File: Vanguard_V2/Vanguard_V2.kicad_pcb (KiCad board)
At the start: 4 copper layers, 55.9 x 30.5 mm, 77 parts, among them IC1 ST1L05CPU33R, IC2 MAX-M10S-00B, IC3 ADXL375BCCZ-RL, IC4 ASM330LHHTR, J1 Conn_01x02_Pin, J2 Conn_01x05_Pin, J3 MEM2067-02-180-00-A, J4 Conn_01x04_Pin, J5 Conn_01x02_Pin, J6 Screw_Terminal_01x04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

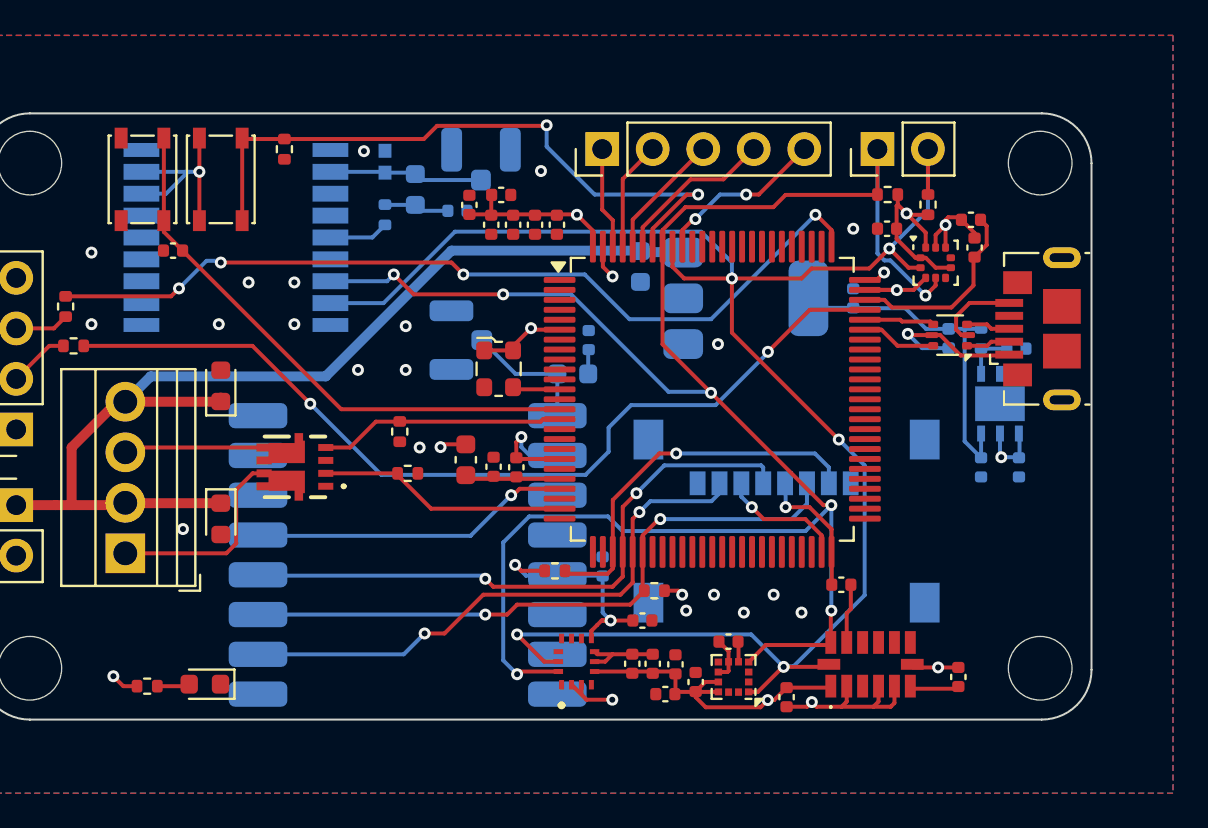
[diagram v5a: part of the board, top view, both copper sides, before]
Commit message: Added ejection charges
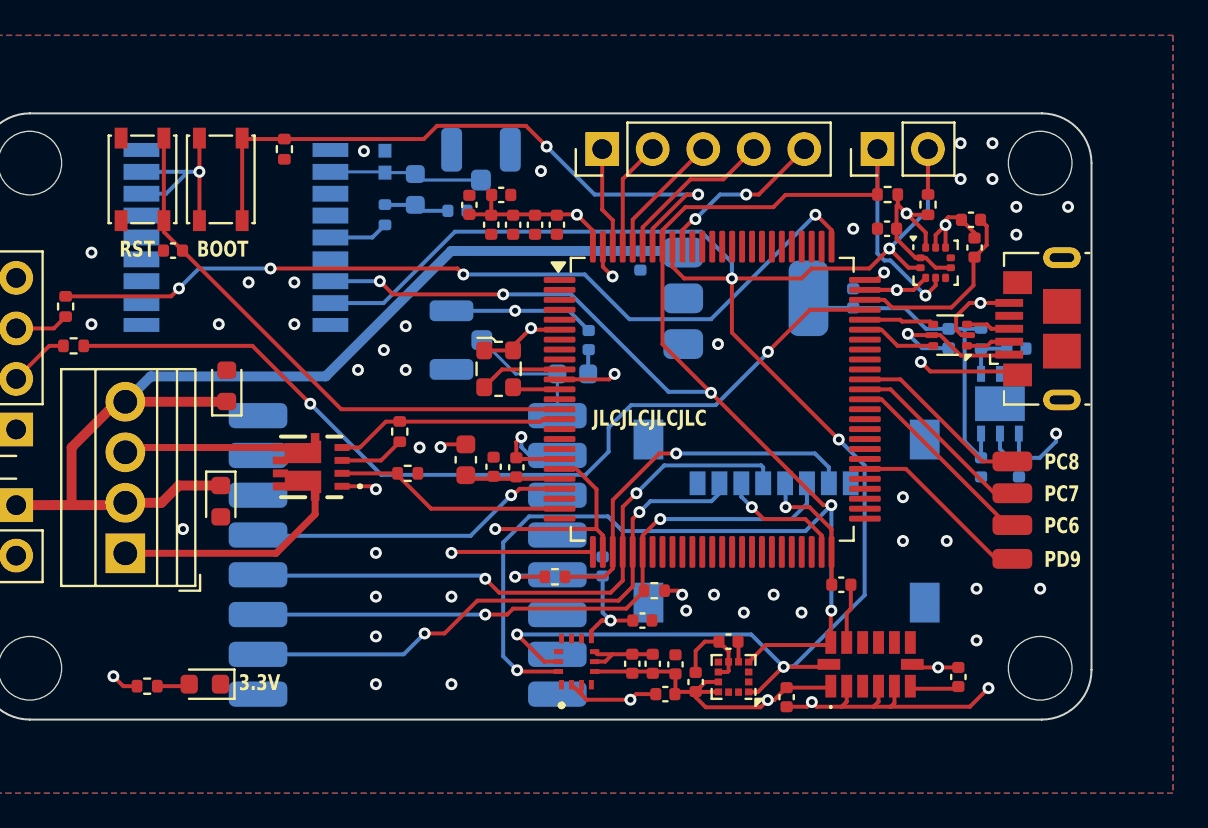
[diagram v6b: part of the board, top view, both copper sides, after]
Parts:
- added TP1: TestPoint, Connector_Wire:SolderWirePad_1x01_SMD_1x2mm, F.Cu at (149.4, 90.0)
- added TP2: TestPoint, Connector_Wire:SolderWirePad_1x01_SMD_1x2mm, F.Cu at (149.4, 91.6)
- added TP3: TestPoint, Connector_Wire:SolderWirePad_1x01_SMD_1x2mm, F.Cu at (149.4, 93.2)
- added TP4: TestPoint, Connector_Wire:SolderWirePad_1x01_SMD_1x2mm, F.Cu at (149.4, 94.9)
- C7: footprint Capacitor_SMD:C_0603_1608Metric -> Capacitor_SMD:C_0402_1005Metric
- moved D4 0.89 mm to (109.6, 92.0)
- moved Q1 0.82 mm to (114.2, 90.3)
- moved D5 0.30 mm to (109.9, 86.2)
- moved C7 0.30 mm to (130.7, 79.9)
- moved R7 0.30 mm to (126.4, 95.8)
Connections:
- Q1 pad 15: unconnected-(Q1-D1_6-Pad15) -> C1_M
- Q1 pad 16: unconnected-(Q1-D2_6-Pad16) -> C2_M
- U1 pad 56: unconnected-(U1-PD9-Pad56) -> Net-(U1-PD9)
- U1 pad 63: unconnected-(U1-PC6-Pad63) -> Net-(U1-PC6)
- U1 pad 64: unconnected-(U1-PC7-Pad64) -> Net-(U1-PC7)
- U1 pad 65: unconnected-(U1-PC8-Pad65) -> Net-(U1-PC8)
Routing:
- net GND: track 48.5 -> 87.3 mm, vias 27 -> 53
- net +3.3V: track 77.7 -> 93.3 mm, vias 14 -> 16
- net Net-(U1-PC6): track 0.00 -> 10.0 mm
- net Net-(U1-PC7): track 0.00 -> 9.58 mm
- net Net-(U1-PD9): track 0.00 -> 9.29 mm
- net Net-(U1-PC8): track 0.00 -> 9.12 mm
- net C1_M: track 10.1 -> 11.8 mm
- net C2_GATE: track 12.3 -> 11.5 mm
- net C2_M: track 7.00 -> 7.82 mm
- net C1_P: track 52.8 -> 53.6 mm
- net C1_GATE: track 12.5 -> 11.8 mm
- net BOOT0: track 33.4 -> 32.7 mm
- net I2C1_SDA: track 101.3 -> 100.7 mm
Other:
- board text added: "3.3V"
- board text added: "BOOT"
- board text added: "JLCJLCJLCJLC"
- board text added: "PC6"
- board text added: "PC7"
- board text added: "PC8"
- board text added: "PD9"
- board text added: "RST"

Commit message: Fixed sensors
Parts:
- added D7: CDBU0520, Resistor_SMD:R_0402_1005Metric, B.Cu at (128.5, 79.4)
- moved C9 25.8 mm to (143.0, 94.7), turned to 0 degrees
- moved C2 19.5 mm to (138.8, 96.7), turned to 180 degrees
- moved C14 17.3 mm to (124.7, 93.9), turned to -90 degrees
- moved C13 5.31 mm to (122.4, 82.4), turned to 180 degrees
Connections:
- C22 pad 1: Net-(IC3-VS) -> +3.3V
- C22 pad 2: +3.3V -> GND
- C7 pad 1: C1_P -> VBATT
- IC3 pad 6: Net-(IC3-VS) -> +3.3V
- IC4 pad 12: unconnected-(IC4-CS-Pad12) -> +3.3V
- U1 pad 89: unconnected-(U1-PB3-Pad89) -> SERVO_5_PWM
- U1 pad 90: unconnected-(U1-PB4-Pad90) -> SERVO_4_PWM
- U1 pad 91: SERVO_5_PWM -> SERVO_3_PWM
- U1 pad 95: SERVO_4_PWM -> SERVO_2_PWM
- U1 pad 96: SERVO_3_PWM -> SERVO_1_PWM
- U1 pad 97: SERVO_2_PWM -> unconnected-(U1-PE0-Pad97)
- U1 pad 98: SERVO_1_PWM -> unconnected-(U1-PE1-Pad98)
- U2 pad 3: C1_P -> VBATT
- U4 pad 5: unconnected-(U4-SA0-Pad5) -> +3.3V
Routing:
- net +3.3V: track 93.3 -> 105.0 mm
- net C1_P: track 53.6 -> 48.7 mm
- net BOOT0: track 32.7 -> 28.3 mm
- net C1_M: track 11.8 -> 15.9 mm
- net VBATT: track 0.00 -> 3.86 mm
- net Net-(IC3-VS): track 2.46 -> 0.00 mm
- net SERVO_4_PWM: track 8.19 -> 6.67 mm, vias 0 -> 1
- net Net-(C1-Pad1): track 9.76 -> 11.2 mm
- net C2_M: track 7.82 -> 9.21 mm
- net SERVO_3_PWM: track 6.38 -> 5.34 mm, vias 0 -> 1
- net GND: track 87.3 -> 88.4 mm, vias 53 -> 67
- net I2C1_SDA: track 100.7 -> 101.2 mm
- net SERVO_5_PWM: track 8.65 -> 8.22 mm, vias 2 -> 1
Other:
- board text added: "B+"
- board text added: "B-"
- board text added: "C1+"
- board text added: "C1-"
- board text added: "C2+"
- board text added: "C2-"
- board text added: "S1"
- board text added: "S2"
- board text added: "S3"
- board text added: "S4"
- board text added: "S5"
- board text added: "SCL"
- board text added: "SDA"

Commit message: added more silkscreen
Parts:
- moved C8 1.00 mm to (141.4, 82.8), turned to -90 degrees
- moved C15 0.83 mm to (149.2, 83.6), turned to -90 degrees
- moved R3 0.66 mm to (147.6, 83.2), turned to 0 degrees
- moved J4 0.52 mm to (99.2, 87.9)
- moved TP4 0.10 mm to (149.4, 94.8)
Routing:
- net GND: track 88.4 -> 92.7 mm, vias 67 -> 69
- net C1_M: track 15.9 -> 14.3 mm
- net Net-(IC1-EN): track 2.57 -> 3.64 mm
- net BOOT0: track 28.3 -> 29.4 mm
- net +5V: track 17.3 -> 16.5 mm
- net C1_P: track 48.7 -> 48.2 mm
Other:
- board text added: "X"
- board text added: "Y"
- board text added: "Z"
